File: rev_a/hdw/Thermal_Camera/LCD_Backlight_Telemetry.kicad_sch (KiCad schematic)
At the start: 0 parts

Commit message: duplicated telemetry for all rails, added random tweaks to logic levels of signals
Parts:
- added C501, C502, C503: 0.1uF, Capacitors_SMD:C_0603, symbol Custom_Library:C_Custom
- added DOC501, DOC502: TBD, symbol Custom_Library:I2C_Address
- added U502: MCP9804, Package_DFN_QFN:DFN-8-1EP_3x2mm_P0.5mm_EP1.3x1.5mm, symbol Sensor_Temperature:MCP9804_DFN
- added U?: INA231A, Custom Footprints Library:Texas_DSBGA-12_1.65x1.39mm_Layout3x4_P0.4mm, symbol Custom Library:INA231A
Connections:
- new net +3.0V: C502.1, C503.1, U502.8 (V_{DD}), U?.B1 (VS)
- new net GND: C502.2, C503.2, U502.4 (GND), U502.9 (EP/GND), U?.C1 (GND)
- new net I2C_SCL: U502.2 (SCL), U?.A1 (SCL)
- new net I2C_SDA: U502.1 (SDA), U?.A2 (SDA)
- new net VLED: U?.D1 (BUS)
- new net VLED_SNS+: C501.1, U?.D3 (IN+)
- new net VLED_SNS-: C501.2, U?.D2 (IN-)
- no-connect marks 0 -> 2
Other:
- note added: "Max Current = 3.1A RSHUNT = 0.02 Ohm CLSB = 9.46045E-05A CAL Register = 0x0A92"

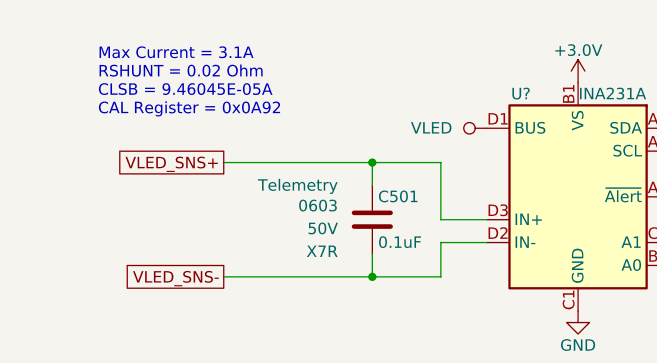
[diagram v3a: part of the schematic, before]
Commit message: added battery circuitry, LCD backlight
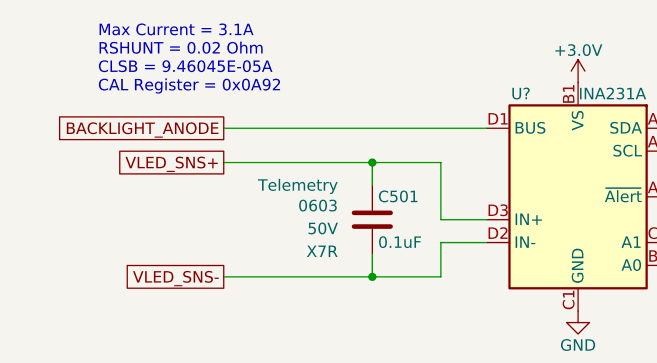
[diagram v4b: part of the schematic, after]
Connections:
- net VLED renamed BACKLIGHT_ANODE
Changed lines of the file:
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@@
+    (stroke (width 0) (type default))
+  )
+  (wire (pts (xy 96.52 41.91) (xy 125.73 41.91))
     (stroke (width 0) (type default))
   )
@@
   )
   (text "Max Current = 3.1A\nRSHUNT = 0.02 Ohm\nCLSB = 9.46045E-05A\nCAL Register = 0x0A92"
-    (at 82.55 40.64 0)
+    (at 82.55 38.1 0)
     (effects (font (size 1.27 1.27)) (justify left bottom))
   )
@@
     )
   )
+  (global_label "BACKLIGHT_ANODE" (shape passive) (at 96.52 41.91 180) (fields_autoplaced)
+    (effects (font (size 1.27 1.27)) (justify right))
+    (property "Intersheetrefs" "${INTERSHEET_REFS}" (at 77.4897 41.91 0)
+      (effects (font (size 1.27 1.27)) (justify right) hide)
+    )
+  )
   (global_label "I2C_SDA" (shape bidirectional) (at 146.05 107.95 0) (fields_autoplaced)
     (effects (font (size 1.27 1.27)) (justify left))
@@
         (path "/4bd21e0b-5408-4b93-866e-c82ac5b31fa9/62eeb8ea-0624-4e55-957b-7df5ce00f512"
           (reference "#PWR01302") (unit 1)
-        )
-      )
-    )
-  )
-  (symbol (lib_id "Custom Library:VLED") (at 125.73 41.91 90) (unit 1)
-    (in_bom yes) (on_board yes) (dnp no)
-    (property "Reference" "#PWR01310" (at 129.54 41.91 0)
-      (effects (font (size 1.27 1.27)) hide)
-    )
-    (property "Value" "VLED" (at 121.92 41.91 90)
-      (effects (font (size 1.27 1.27)) (justify left))
-    )
-    (property "Footprint" "" (at 125.73 41.91 0)
-      (effects (font (size 1.27 1.27)) hide)
-    )
-    (property "Datasheet" "" (at 125.73 41.91 0)
-      (effects (font (size 1.27 1.27)) hide)
-    )
-    (pin "1")
-    (instances
-      (project "Thermal_Camera"
-        (path "/4bd21e0b-5408-4b93-866e-c82ac5b31fa9/62eeb8ea-0624-4e55-957b-7df5ce00f512"
-          (reference "#PWR01310") (unit 1)
         )
       )
@@
       (effects (font (size 1.27 1.27)) hide)
     )
-    (pin "B1")
-    (pin "C2")
     (pin "A1")
     (pin "A2")
     (pin "A3")
+    (pin "B1")
+    (pin "B2")
     (pin "B3")
     (pin "C1")
+    (pin "C2")
     (pin "C3")
-    (pin "B2")
+    (pin "D1")
     (pin "D2")
     (pin "D3")
-    (pin "D1")
-    (instances
-      (project "Thermal_Camera"
+    (instances
+      (project "Thermal_Camera"

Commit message: lots of schematic progress
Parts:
- C?: renamed from C501; footprint Capacitors_SMD:C_0603 -> (none); Digi-Key PN 1276-1935-1-ND -> (none); display_footprint 0603 -> (none)
- C?: renamed from C502; footprint Capacitors_SMD:C_0603 -> (none); Digi-Key PN 1276-1935-1-ND -> (none); display_footprint 0603 -> (none)
- C?: renamed from C503; footprint Capacitors_SMD:C_0603 -> (none); Digi-Key PN 1276-1935-1-ND -> (none); display_footprint 0603 -> (none)
- DOC?: renamed from DOC501; value TBD -> 0x75
- DOC?: renamed from DOC502; value TBD -> 0x1D
- gave numbers to parts that had none: 1
- renumbered U502 to U?
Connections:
- net +3.0V: now also U1301.B3 (A0), U1301.C3 (A1), U?.5 (A2), U?.7 (A0)
- net GND: now also U?.6 (A1)

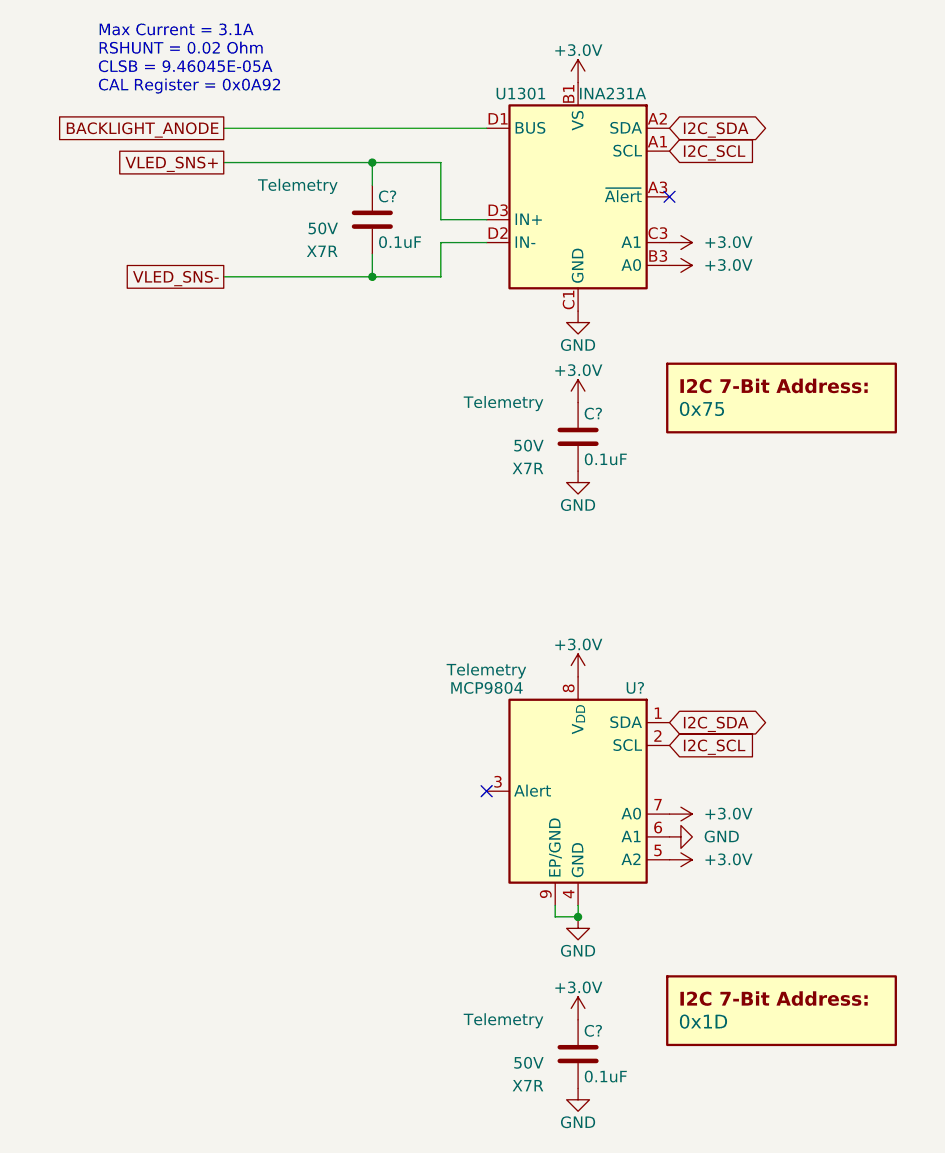
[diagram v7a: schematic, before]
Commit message: assigned a ton of footprints
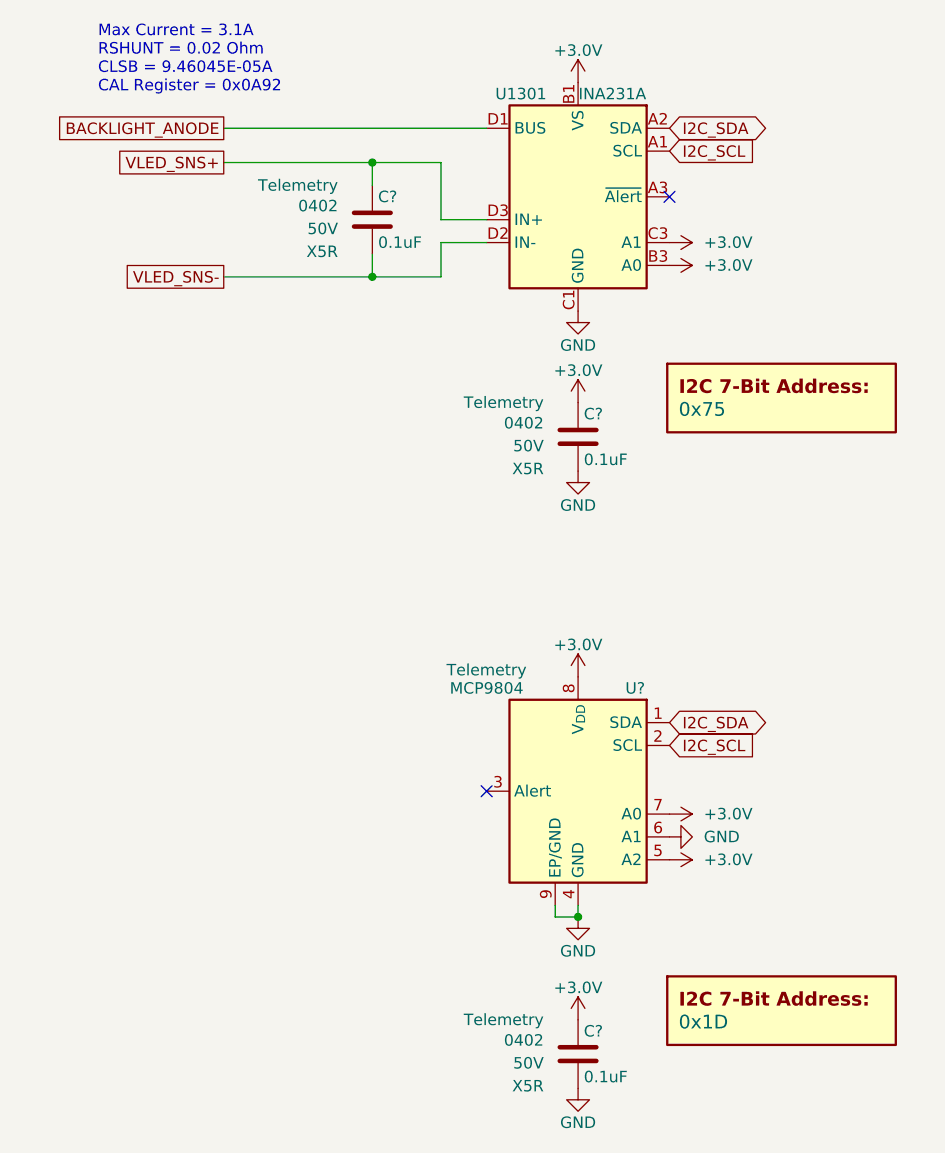
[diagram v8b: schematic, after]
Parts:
- C? (x3): footprint (none) -> Capacitors_SMD:C_0402; Dielectric X7R -> X5R; display_footprint (none) -> 0402
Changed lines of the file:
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@@
 			)
 		)
-		(property "Footprint" ""
+		(property "Footprint" "Capacitors_SMD:C_0402"
 			(at 113.9952 55.88 0)
 			(effects
@@
 			)
 		)
-		(property "display_footprint" ""
+		(property "display_footprint" "0402"
 			(at 109.22 50.546 0)
 			(effects
@@
 			)
 		)
-		(property "Dielectric" "X7R"
+		(property "Dielectric" "X5R"
 			(at 109.22 55.626 0)
 			(effects
@@
 			)
 		)
-		(property "Footprint" ""
+		(property "Footprint" "Capacitors_SMD:C_0402"
 			(at 136.8552 80.01 0)
 			(effects
@@
 			)
 		)
-		(property "display_footprint" ""
+		(property "display_footprint" "0402"
 			(at 132.08 74.676 0)
 			(effects
@@
 			)
 		)
-		(property "Dielectric" "X7R"
+		(property "Dielectric" "X5R"
 			(at 132.08 79.756 0)
 			(effects
@@
 			)
 		)
-		(property "Footprint" ""
+		(property "Footprint" "Capacitors_SMD:C_0402"
 			(at 136.8552 148.59 0)
 			(effects
@@
 			)
 		)
-		(property "display_footprint" ""
+		(property "display_footprint" "0402"
 			(at 132.08 143.256 0)
 			(effects
@@
 			)
 		)
-		(property "Dielectric" "X7R"
+		(property "Dielectric" "X5R"
 			(at 132.08 148.336 0)
 			(effects
